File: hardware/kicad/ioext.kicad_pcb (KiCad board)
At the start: 2 copper layers, 66 x 51 mm, 50 parts, among them P1 CONN_01X04, P2 CONN_02X08, P3 CONN_01X10, Q1 IRLZ44N, Q2 IRLZ44N, Q3 IRLZ44N, Q4 IRLZ44N, Q5 IRLZ44N, Q6 IRLZ44N, Q7 IRLZ44N, Q8 IRLZ44N, U1 PCF8574A, U2 PC817, U3 PC817, U4 PC817, U5 PC817, U6 PC817, U7 PC817, U8 PC817, U9 PC817

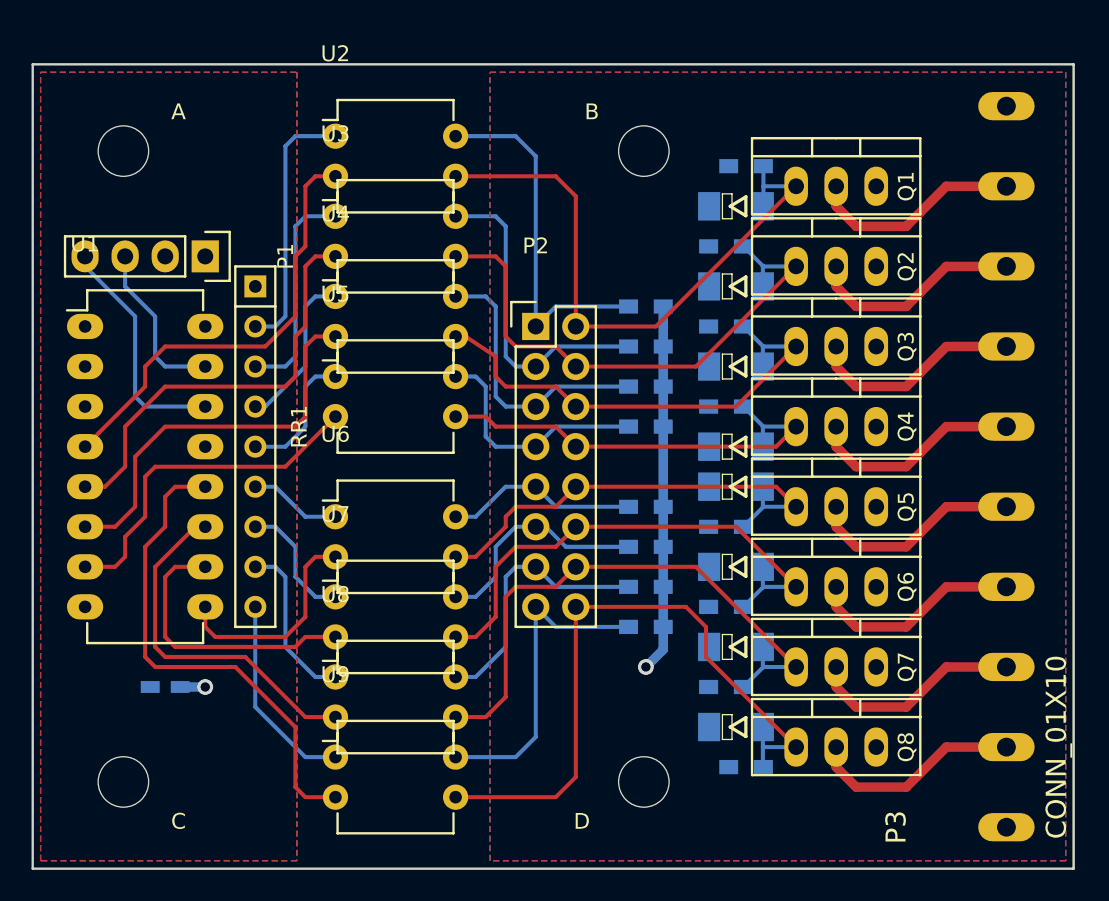
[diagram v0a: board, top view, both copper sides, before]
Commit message: hardware/kicad ioext: use 3x jumper block insterad of inidividual jumpers
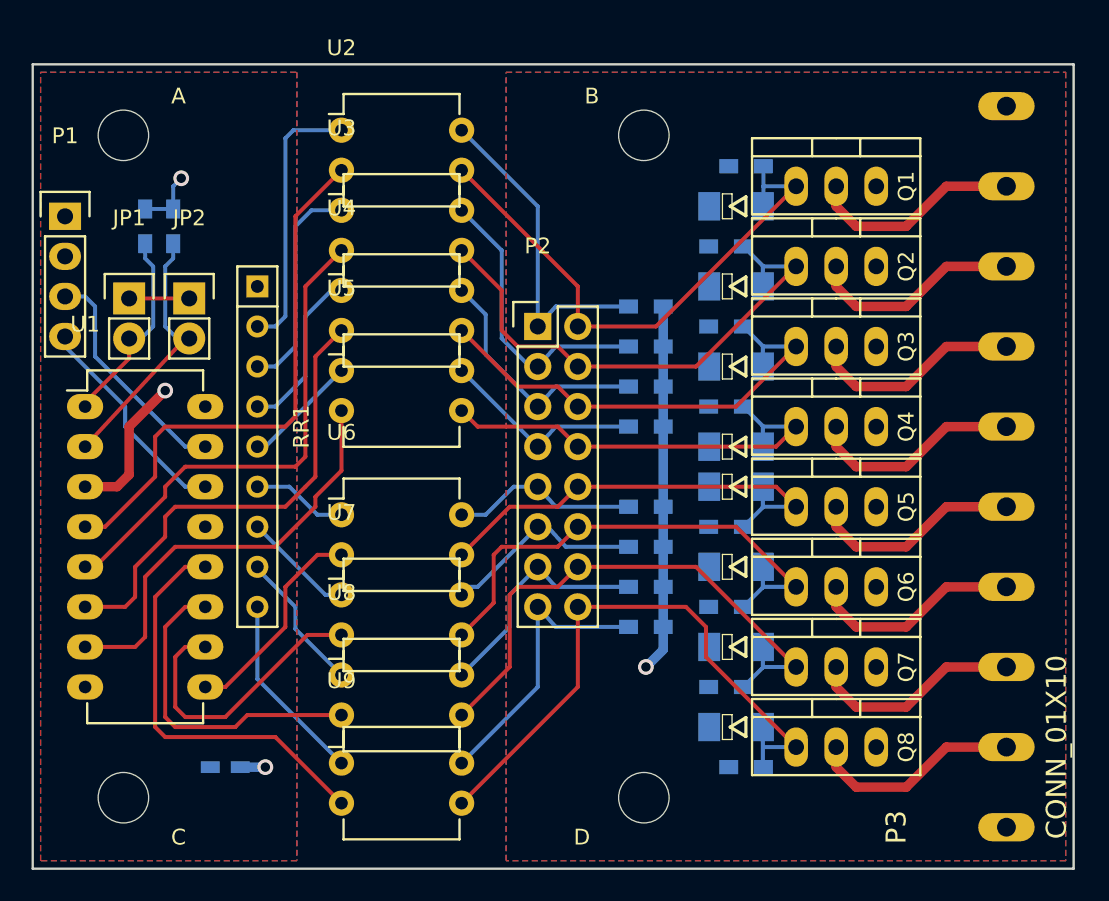
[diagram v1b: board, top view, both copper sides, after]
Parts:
- added JP1: Jumper_NC_Small, Pin_Headers:Pin_Header_Straight_1x02, F.Cu at (213.6, 101.1)
- added JP2: Jumper_NC_Small, Pin_Headers:Pin_Header_Straight_1x02, F.Cu at (217.4, 101.1)
- added R17: 10k, Resistors_SMD:R_0603_HandSoldering, B.Cu at (214.6, 96.5)
- added R18: 10k, Resistors_SMD:R_0603_HandSoldering, B.Cu at (216.4, 96.5)
- moved P1 9.25 mm to (209.6, 95.9), turned to 0 degrees
- moved C1 6.35 mm to (219.7, 130.8)
- moved U1 5.08 mm to (210.8, 108.0)
- moved A 1.00 mm to (213.2, 90.8)
- moved B 1.00 mm to (246.2, 90.8)
- moved C 1.00 mm to (213.2, 132.8)
- moved D 1.00 mm to (246.2, 132.8)
- moved U2 0.54 mm to (227.1, 90.4)
- moved U3 0.54 mm to (227.1, 95.5)
- moved U4 0.54 mm to (227.1, 100.6)
- moved U5 0.54 mm to (227.1, 105.7)
- moved U9 0.54 mm to (227.1, 130.6)
- moved U6 0.40 mm to (227.1, 114.8)
- moved U7 0.40 mm to (227.1, 119.9)
- moved U8 0.40 mm to (227.1, 125.0)
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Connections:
- U1 pad 1: GND -> Net-(JP1-Pad2)
- U1 pad 2: GND -> Net-(JP2-Pad2)
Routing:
- net Net-(JP2-Pad2): track 0.00 -> 16.9 mm
- net Net-(JP1-Pad2): track 0.00 -> 13.4 mm
- net GND: track 0.00 -> 13.2 mm, vias 0 -> 1
- net Net-(U1-Pad4): track 28.2 -> 34.5 mm
- net Net-(U1-Pad12): track 31.5 -> 26.0 mm
- net Net-(U1-Pad7): track 22.1 -> 27.3 mm
- net Net-(U1-Pad6): track 25.3 -> 29.8 mm
- net Net-(U1-Pad5): track 27.1 -> 31.3 mm
- net Net-(P1-Pad3): track 10.6 -> 14.7 mm
- net +5V: track 1.59 -> 5.53 mm, vias 1 -> 2
- net Net-(D1-Pad1): track 38.7 -> 35.1 mm
- net Net-(D8-Pad1): track 42.4 -> 38.8 mm
- net Net-(P2-Pad7): track 15.2 -> 13.1 mm
- net Net-(P2-Pad5): track 17.7 -> 15.7 mm
- net Net-(P2-Pad15): track 20.3 -> 18.2 mm
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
